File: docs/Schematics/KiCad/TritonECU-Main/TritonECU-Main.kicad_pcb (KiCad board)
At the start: 4 copper layers, 158 x 174 mm, 48 parts, among them J1 EEC-V 104, Q101 ISL9V3040S3ST, Q102 ISL9V3040S3ST, Q103 ISL9V3040S3ST, Q104 ISL9V3040S3ST, Q105 ISL9V3040S3ST, Q106 ISL9V3040S3ST, Q107 ISL9V3040S3ST, Q108 ISL9V3040S3ST, Q109 BSS138, Q201 ZXMS6005DGQTA, Q202 ZXMS6005DGQTA, Q203 ZXMS6005DGQTA, Q204 ZXMS6005DGQTA, Q205 ZXMS6005DGQTA, Q206 ZXMS6005DGQTA, Q207 ZXMS6005DGQTA, Q208 ZXMS6005DGQTA, U101 74HCT541, U102 TPS3823A-33DBVR

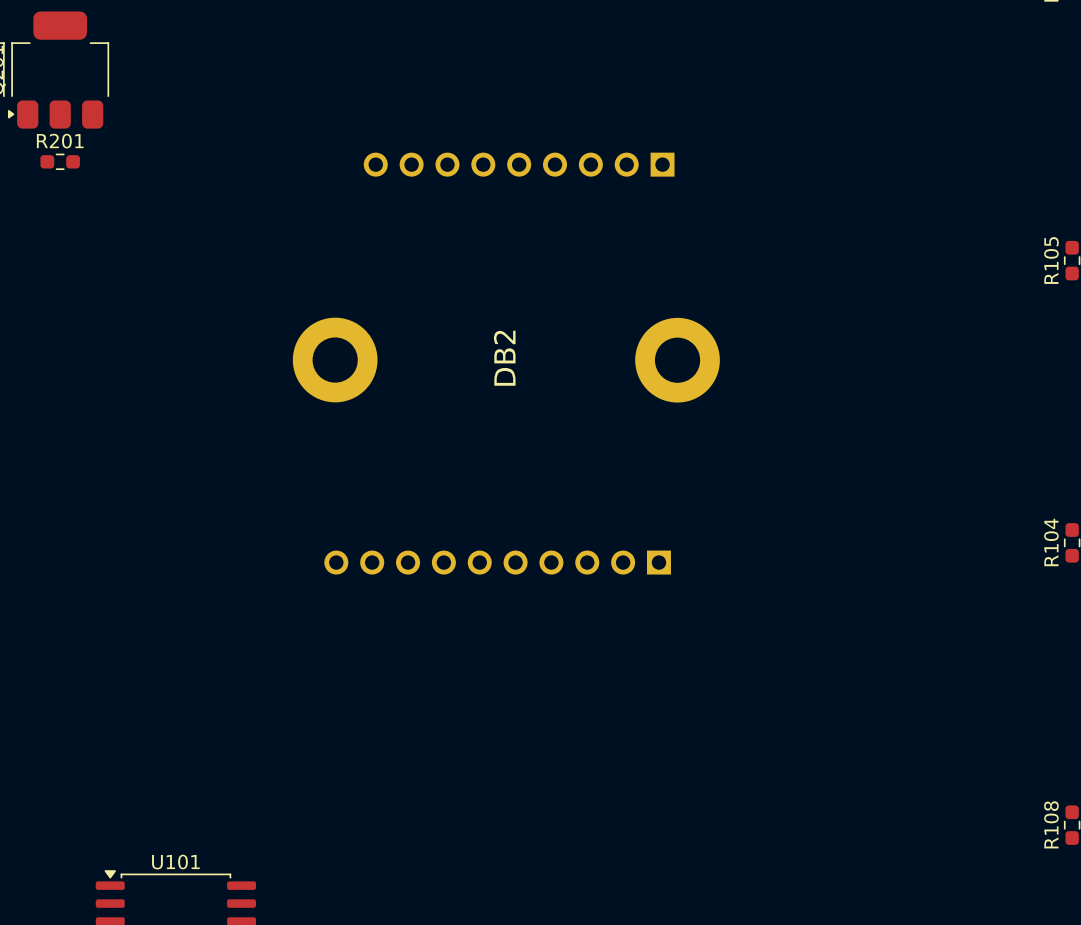
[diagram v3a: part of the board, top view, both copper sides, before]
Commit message: Carrier: VR front end on the main board, 3 x MAX9926
The VR daughterboard (DB2) is removed; the conditioning moves onto the carrier
as Vr.kicad_sch, U301-U303: CKP + spare, CMP + OSS, TSS + transfer case. All
V1 review fixes applied: 2 x 5k 0805 per input leg (300 V), 470 pF C0G 200 V
across the inputs, 100 nF on BIAS, 10n + 100n + 1u per VCC. Single-ended
sensors return on SIGRTN; the CMP shield goes single-point to the star through
R399; the spare channel is on header J301. VR board V1 stays the bench board.

Placed where DB2 was, under the CMP/OSS/TSS/TC pins. ERC 0 errors, PCB
schematic parity clean, no courtyard overlaps.

Generators: lock check ignores the project window alone; stale footprints are
removed after the new ones load (a Remove first broke the footprint loader).

Co-Authored-By: Claude Opus 5.5 <noreply@anthropic.com>
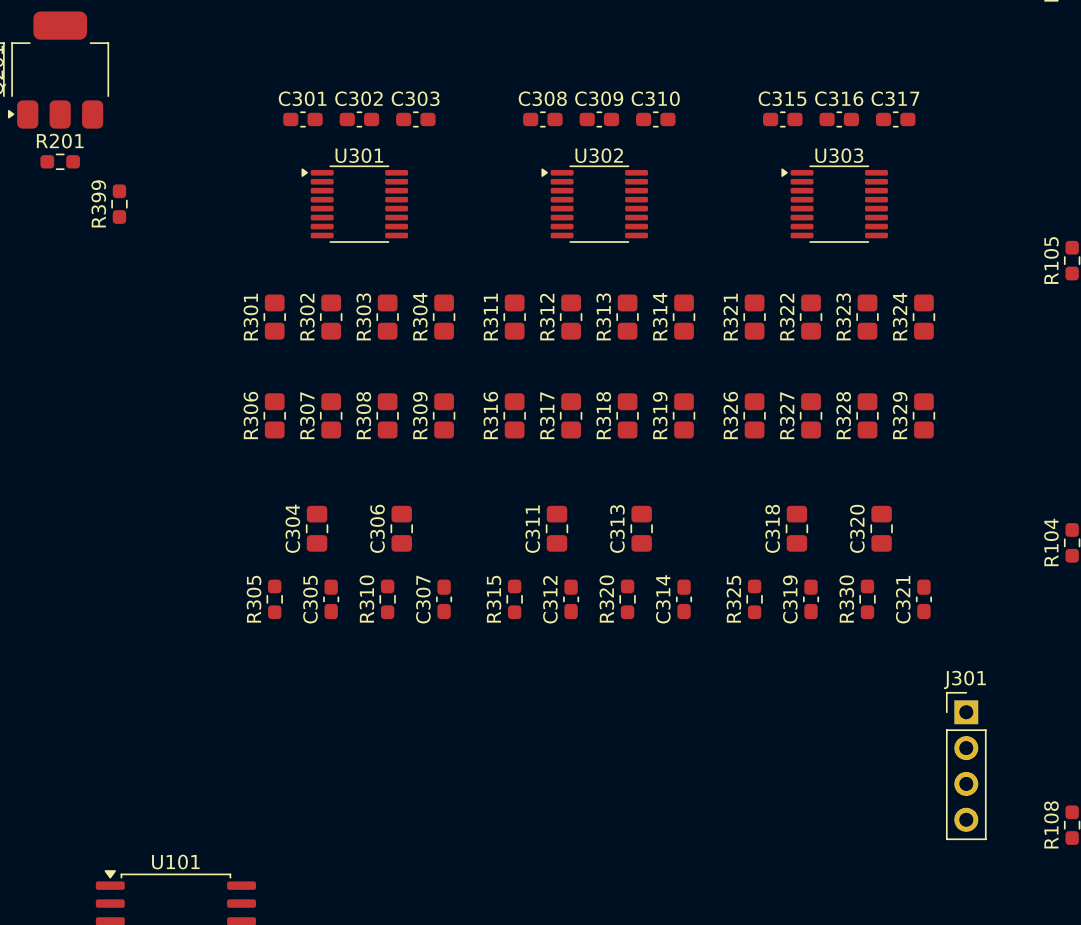
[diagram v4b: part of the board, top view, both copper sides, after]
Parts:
- removed DB2: VR board V1, TritonECU-Main:VRBoard_V1_Mate
- added C301: 10n, Capacitor_SMD:C_0603_1608Metric_Pad1.08x0.95mm_HandSolder, F.Cu at (113.0, 56.0)
- added C302: 100n, Capacitor_SMD:C_0603_1608Metric_Pad1.08x0.95mm_HandSolder, F.Cu at (117.0, 56.0)
- added C303: 1u, Capacitor_SMD:C_0603_1608Metric_Pad1.08x0.95mm_HandSolder, F.Cu at (121.0, 56.0)
- added C304: 470p, Capacitor_SMD:C_0805_2012Metric_Pad1.18x1.45mm_HandSolder, F.Cu at (114.0, 85.0)
- added C305: 100n, Capacitor_SMD:C_0603_1608Metric_Pad1.08x0.95mm_HandSolder, F.Cu at (115.0, 90.0)
- added C306: 470p, Capacitor_SMD:C_0805_2012Metric_Pad1.18x1.45mm_HandSolder, F.Cu at (120.0, 85.0)
- added C307: 100n, Capacitor_SMD:C_0603_1608Metric_Pad1.08x0.95mm_HandSolder, F.Cu at (123.0, 90.0)
- added C308: 10n, Capacitor_SMD:C_0603_1608Metric_Pad1.08x0.95mm_HandSolder, F.Cu at (130.0, 56.0)
- added C309: 100n, Capacitor_SMD:C_0603_1608Metric_Pad1.08x0.95mm_HandSolder, F.Cu at (134.0, 56.0)
- added C310: 1u, Capacitor_SMD:C_0603_1608Metric_Pad1.08x0.95mm_HandSolder, F.Cu at (138.0, 56.0)
- added C311: 470p, Capacitor_SMD:C_0805_2012Metric_Pad1.18x1.45mm_HandSolder, F.Cu at (131.0, 85.0)
- added C312: 100n, Capacitor_SMD:C_0603_1608Metric_Pad1.08x0.95mm_HandSolder, F.Cu at (132.0, 90.0)
- added C313: 470p, Capacitor_SMD:C_0805_2012Metric_Pad1.18x1.45mm_HandSolder, F.Cu at (137.0, 85.0)
- added C314: 100n, Capacitor_SMD:C_0603_1608Metric_Pad1.08x0.95mm_HandSolder, F.Cu at (140.0, 90.0)
- added C315: 10n, Capacitor_SMD:C_0603_1608Metric_Pad1.08x0.95mm_HandSolder, F.Cu at (147.0, 56.0)
- added C316: 100n, Capacitor_SMD:C_0603_1608Metric_Pad1.08x0.95mm_HandSolder, F.Cu at (151.0, 56.0)
- added C317: 1u, Capacitor_SMD:C_0603_1608Metric_Pad1.08x0.95mm_HandSolder, F.Cu at (155.0, 56.0)
- added C318: 470p, Capacitor_SMD:C_0805_2012Metric_Pad1.18x1.45mm_HandSolder, F.Cu at (148.0, 85.0)
- added C319: 100n, Capacitor_SMD:C_0603_1608Metric_Pad1.08x0.95mm_HandSolder, F.Cu at (149.0, 90.0)
- added C320: 470p, Capacitor_SMD:C_0805_2012Metric_Pad1.18x1.45mm_HandSolder, F.Cu at (154.0, 85.0)
- added C321: 100n, Capacitor_SMD:C_0603_1608Metric_Pad1.08x0.95mm_HandSolder, F.Cu at (157.0, 90.0)
- added J301: VR spare, Connector_PinHeader_2.54mm:PinHeader_1x04_P2.54mm_Vertical, F.Cu at (160.0, 98.0)
- added R301: 5k, Resistor_SMD:R_0805_2012Metric_Pad1.20x1.40mm_HandSolder, F.Cu at (111.0, 70.0)
- added R302: 5k, Resistor_SMD:R_0805_2012Metric_Pad1.20x1.40mm_HandSolder, F.Cu at (115.0, 70.0)
- added R303: 5k, Resistor_SMD:R_0805_2012Metric_Pad1.20x1.40mm_HandSolder, F.Cu at (119.0, 70.0)
- added R304: 5k, Resistor_SMD:R_0805_2012Metric_Pad1.20x1.40mm_HandSolder, F.Cu at (123.0, 70.0)
- added R305: 10k, Resistor_SMD:R_0603_1608Metric_Pad0.98x0.95mm_HandSolder, F.Cu at (111.0, 90.0)
- added R306: 5k, Resistor_SMD:R_0805_2012Metric_Pad1.20x1.40mm_HandSolder, F.Cu at (111.0, 77.0)
- added R307: 5k, Resistor_SMD:R_0805_2012Metric_Pad1.20x1.40mm_HandSolder, F.Cu at (115.0, 77.0)
- added R308: 5k, Resistor_SMD:R_0805_2012Metric_Pad1.20x1.40mm_HandSolder, F.Cu at (119.0, 77.0)
- added R309: 5k, Resistor_SMD:R_0805_2012Metric_Pad1.20x1.40mm_HandSolder, F.Cu at (123.0, 77.0)
- added R310: 10k, Resistor_SMD:R_0603_1608Metric_Pad0.98x0.95mm_HandSolder, F.Cu at (119.0, 90.0)
- added R311: 5k, Resistor_SMD:R_0805_2012Metric_Pad1.20x1.40mm_HandSolder, F.Cu at (128.0, 70.0)
- added R312: 5k, Resistor_SMD:R_0805_2012Metric_Pad1.20x1.40mm_HandSolder, F.Cu at (132.0, 70.0)
- added R313: 5k, Resistor_SMD:R_0805_2012Metric_Pad1.20x1.40mm_HandSolder, F.Cu at (136.0, 70.0)
- added R314: 5k, Resistor_SMD:R_0805_2012Metric_Pad1.20x1.40mm_HandSolder, F.Cu at (140.0, 70.0)
- added R315: 10k, Resistor_SMD:R_0603_1608Metric_Pad0.98x0.95mm_HandSolder, F.Cu at (128.0, 90.0)
- added R316: 5k, Resistor_SMD:R_0805_2012Metric_Pad1.20x1.40mm_HandSolder, F.Cu at (128.0, 77.0)
- added R317: 5k, Resistor_SMD:R_0805_2012Metric_Pad1.20x1.40mm_HandSolder, F.Cu at (132.0, 77.0)
- added R318: 5k, Resistor_SMD:R_0805_2012Metric_Pad1.20x1.40mm_HandSolder, F.Cu at (136.0, 77.0)
- added R319: 5k, Resistor_SMD:R_0805_2012Metric_Pad1.20x1.40mm_HandSolder, F.Cu at (140.0, 77.0)
- added R320: 10k, Resistor_SMD:R_0603_1608Metric_Pad0.98x0.95mm_HandSolder, F.Cu at (136.0, 90.0)
- added R321: 5k, Resistor_SMD:R_0805_2012Metric_Pad1.20x1.40mm_HandSolder, F.Cu at (145.0, 70.0)
- added R322: 5k, Resistor_SMD:R_0805_2012Metric_Pad1.20x1.40mm_HandSolder, F.Cu at (149.0, 70.0)
- added R323: 5k, Resistor_SMD:R_0805_2012Metric_Pad1.20x1.40mm_HandSolder, F.Cu at (153.0, 70.0)
- added R324: 5k, Resistor_SMD:R_0805_2012Metric_Pad1.20x1.40mm_HandSolder, F.Cu at (157.0, 70.0)
- added R325: 10k, Resistor_SMD:R_0603_1608Metric_Pad0.98x0.95mm_HandSolder, F.Cu at (145.0, 90.0)
- added R326: 5k, Resistor_SMD:R_0805_2012Metric_Pad1.20x1.40mm_HandSolder, F.Cu at (145.0, 77.0)
- added R327: 5k, Resistor_SMD:R_0805_2012Metric_Pad1.20x1.40mm_HandSolder, F.Cu at (149.0, 77.0)
- added R328: 5k, Resistor_SMD:R_0805_2012Metric_Pad1.20x1.40mm_HandSolder, F.Cu at (153.0, 77.0)
- added R329: 5k, Resistor_SMD:R_0805_2012Metric_Pad1.20x1.40mm_HandSolder, F.Cu at (157.0, 77.0)
- added R330: 10k, Resistor_SMD:R_0603_1608Metric_Pad0.98x0.95mm_HandSolder, F.Cu at (153.0, 90.0)
- added R399: 0, Resistor_SMD:R_0603_1608Metric_Pad0.98x0.95mm_HandSolder, F.Cu at (100.0, 62.0)
- added U301: MAX9926UAEE+T, Package_SO:QSOP-16_3.9x4.9mm_P0.635mm, F.Cu at (117.0, 62.0)
- added U302: MAX9926UAEE+T, Package_SO:QSOP-16_3.9x4.9mm_P0.635mm, F.Cu at (134.0, 62.0)
- added U303: MAX9926UAEE+T, Package_SO:QSOP-16_3.9x4.9mm_P0.635mm, F.Cu at (151.0, 62.0)
